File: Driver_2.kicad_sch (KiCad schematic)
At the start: 34 parts

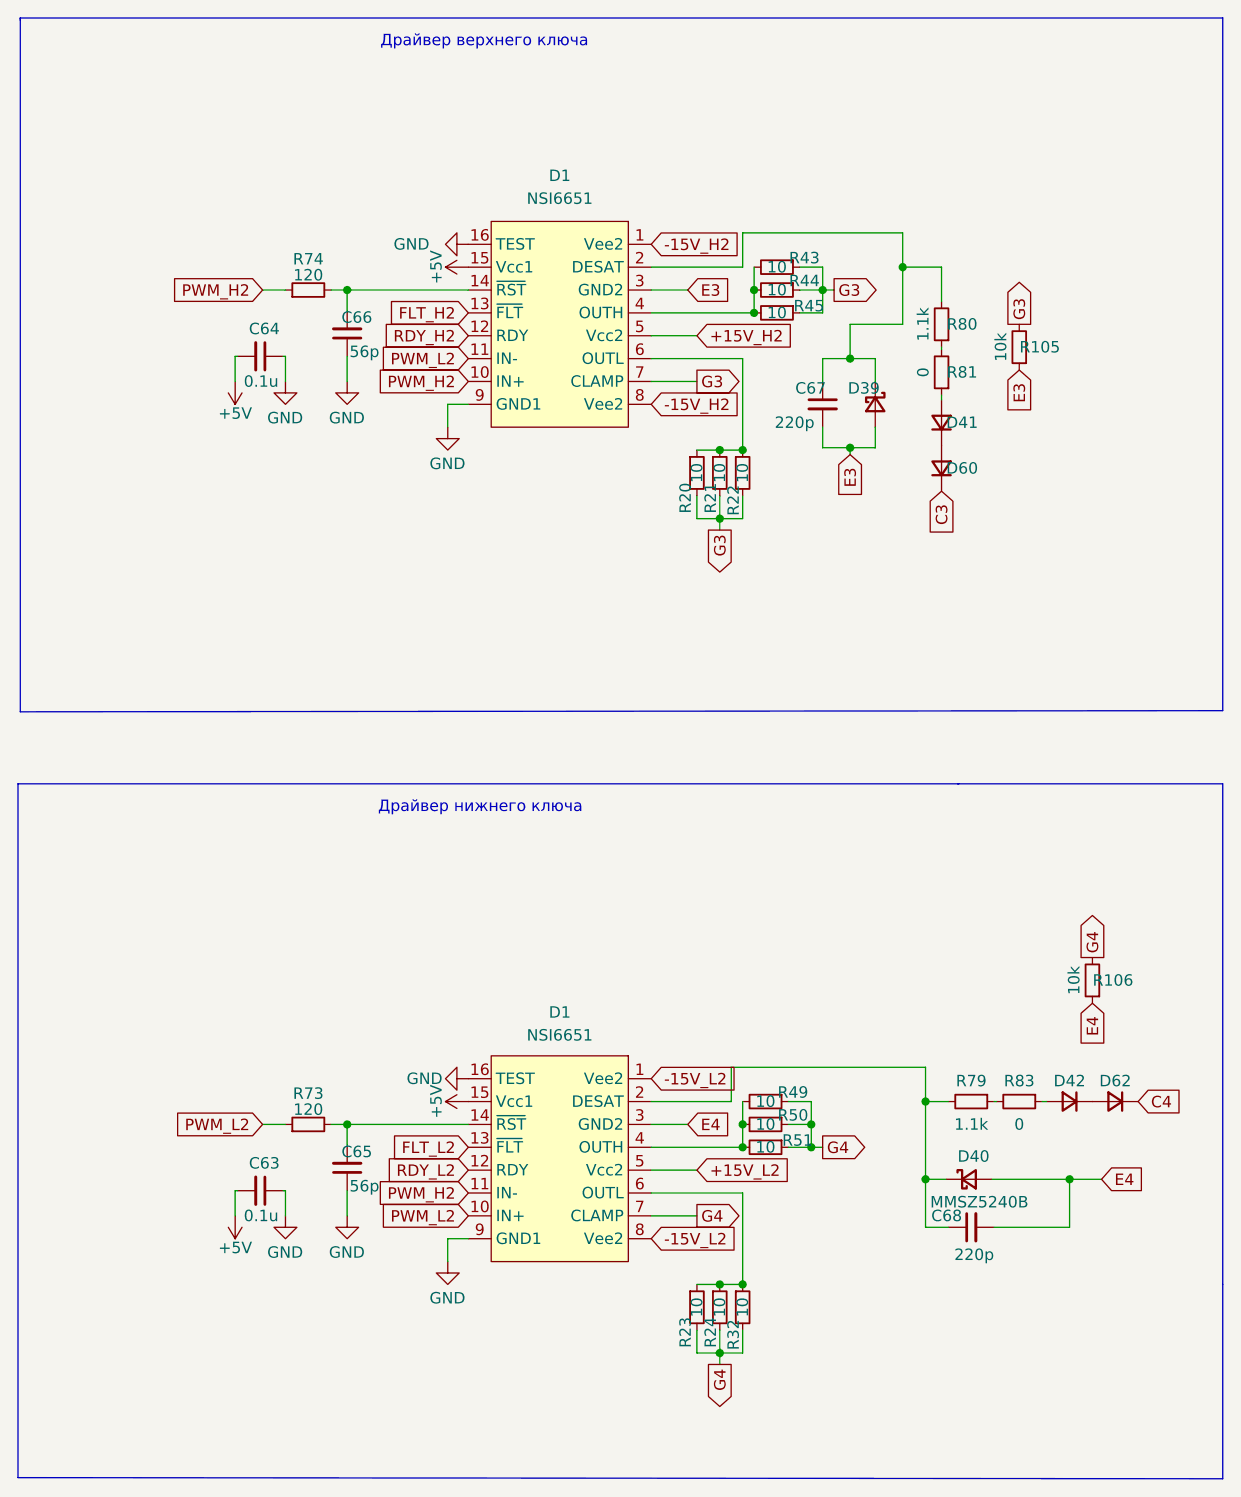
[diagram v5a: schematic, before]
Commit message: Развел стойку фазы А
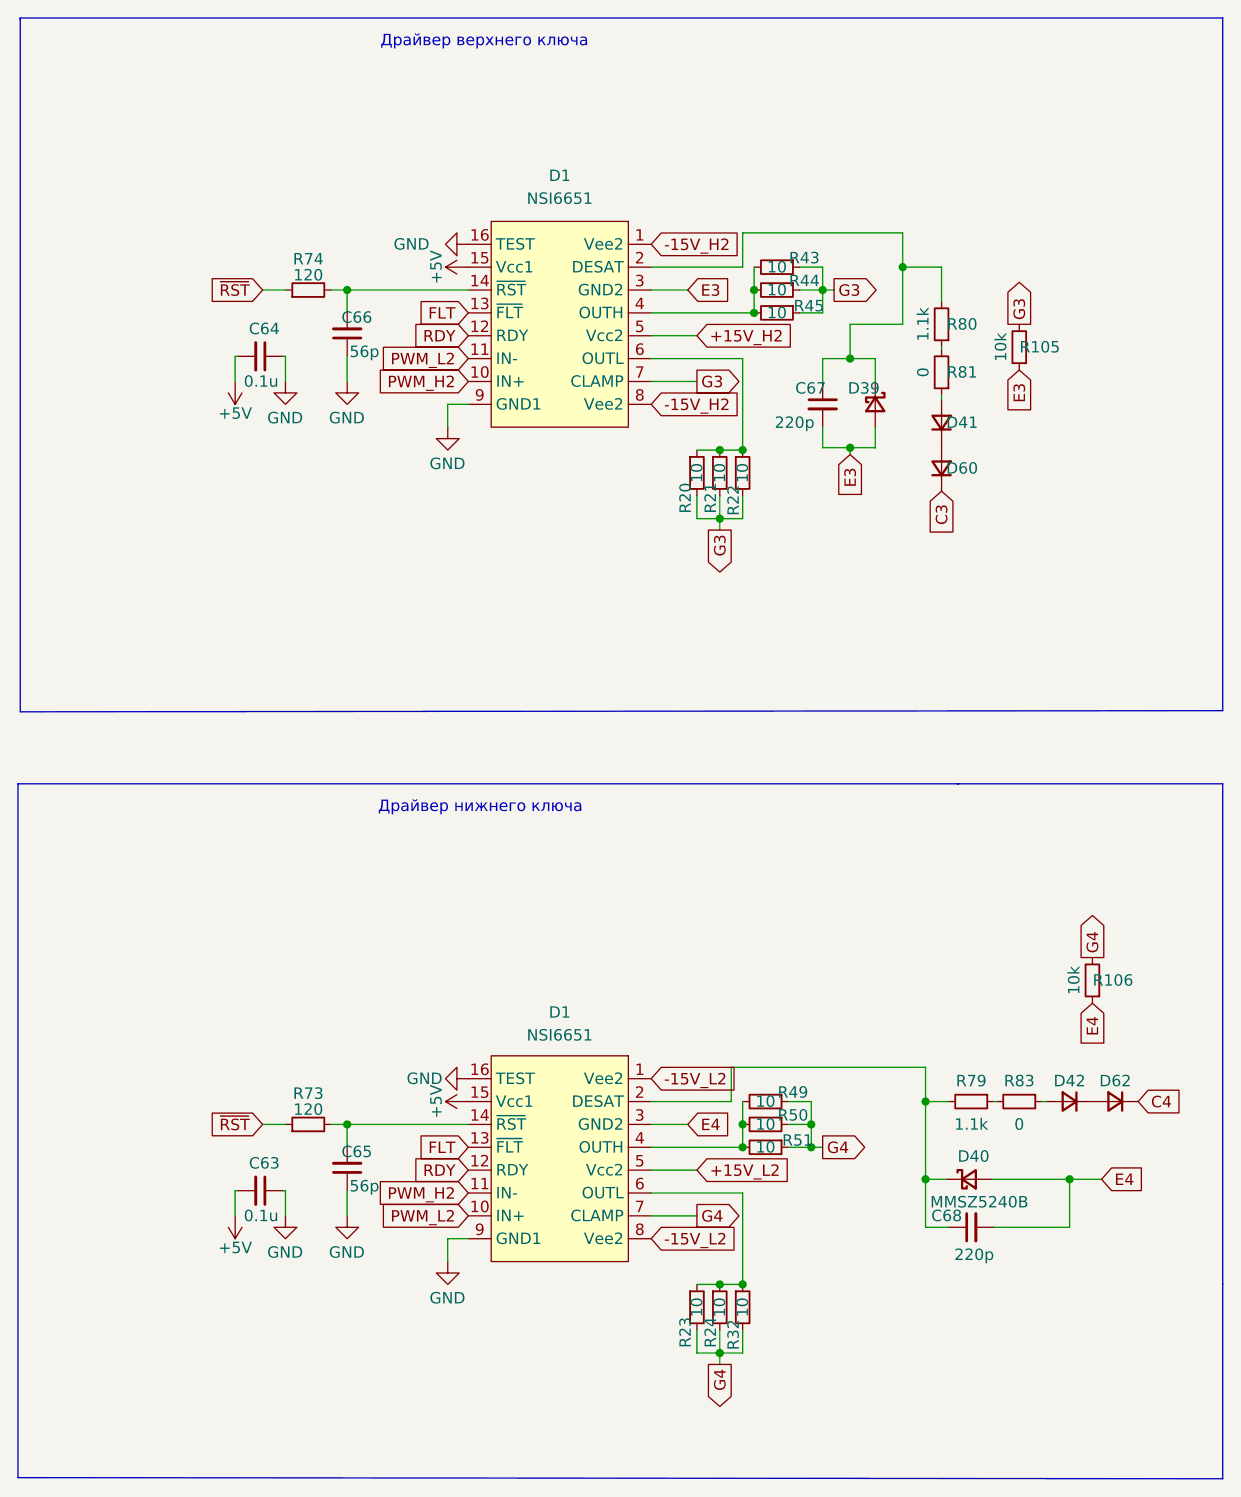
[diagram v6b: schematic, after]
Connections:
- net FLT_L2 is gone; now on net FLT: D1.13 (~{FLT})
- net RDY_L2 is gone; now on net RDY: D1.12 (RDY)
- net PWM_H2: no longer R74.1
- net PWM_L2: no longer R73.1
- net FLT_H2 renamed FLT
- net RDY_H2 renamed RDY
- new net ~{RST}: R73.1, R74.1
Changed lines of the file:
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@@
 		)
 	)
-	(global_label "FLT_H2"
+	(global_label "FLT"
 		(shape input)
 		(at 81.28 55.88 180)
@@
 		)
 		(property "Intersheetrefs" "${INTERSHEET_REFS}"
-			(at 72.275 55.8006 0)
+			(at 75.7206 55.88 0)
 			(effects
 				(font
@@
 		)
 	)
-	(global_label "FLT_L2"
+	(global_label "FLT"
 		(shape input)
 		(at 81.28 148.59 180)
@@
 		)
 		(property "Intersheetrefs" "${INTERSHEET_REFS}"
-			(at 72.5774 148.5106 0)
+			(at 75.7206 148.59 0)
 			(effects
 				(font
@@
 		)
 	)
-	(global_label "RDY_H2"
+	(global_label "RDY"
 		(shape input)
 		(at 81.28 58.42 180)
@@
 		)
 		(property "Intersheetrefs" "${INTERSHEET_REFS}"
-			(at 71.7307 58.3406 0)
+			(at 75.3384 58.42 0)
 			(effects
 				(font
@@
 		)
 	)
-	(global_label "RDY_L2"
+	(global_label "RDY"
 		(shape input)
 		(at 81.28 151.13 180)
@@
 		)
 		(property "Intersheetrefs" "${INTERSHEET_REFS}"
-			(at 72.0331 151.0506 0)
+			(at 75.3384 151.13 0)
 			(effects
 				(font
@@
 	(global_label "PWM_L2"
 		(shape input)
-		(at 58.42 146.05 180)
-		(fields_autoplaced yes)
-		(effects
-			(font
-				(size 1.27 1.27)
-			)
-			(justify right)
-		)
-		(property "Intersheetrefs" "${INTERSHEET_REFS}"
-			(at 48.6288 145.9706 0)
-			(effects
-				(font
-					(size 1.27 1.27)
-				)
-				(justify right)
-				(hide yes)
-			)
-		)
-	)
-	(global_label "PWM_L2"
-		(shape input)
 		(at 81.28 60.96 180)
 		(fields_autoplaced yes)
@@
 		)
 	)
-	(global_label "PWM_H2"
+	(global_label "~{RST}"
 		(shape input)
-		(at 58.42 53.34 180)
+		(at 58.42 146.05 180)
 		(fields_autoplaced yes)
 		(effects
@@
 		)
 		(property "Intersheetrefs" "${INTERSHEET_REFS}"
-			(at 48.3264 53.2606 0)
+			(at 52.605 146.05 0)
 			(effects
 				(font
@@
 		)
 	)
+	(global_label "~{RST}"
+		(shape input)
+		(at 58.42 53.34 180)
+		(fields_autoplaced yes)
+		(effects
+			(font
+				(size 1.27 1.27)
+			)
+			(justify right)
+		)
+		(property "Intersheetrefs" "${INTERSHEET_REFS}"
+			(at 52.605 53.34 0)
+			(effects
+				(font
+					(size 1.27 1.27)
+				)
+				(justify right)
+				(hide yes)
+			)
+		)
+	)
 	(global_label "-15V_H2"
 		(shape input)
@@
 		(on_board yes)
 		(dnp no)
-		(property "Reference" "#PWR181"
+		(property "Reference" "#PWR0181"
 			(at 55.372 152.4 0)
 			(effects
@@
 			(project "Adapter"
 				(path "/e63e39d7-6ac0-4ffd-8aa3-1841a4541b55/7be86f5d-dd1f-4f1b-8cd0-4746349973df"
-					(reference "#PWR181")
+					(reference "#PWR0181")
 					(unit 1)
 				)
@@
 		(on_board yes)
 		(dnp no)
-		(property "Reference" "#PWR176"
+		(property "Reference" "#PWR0176"
 			(at 85.09 50.8 0)
 			(effects
@@
 			(project "Adapter"
 				(path "/e63e39d7-6ac0-4ffd-8aa3-1841a4541b55/7be86f5d-dd1f-4f1b-8cd0-4746349973df"
-					(reference "#PWR176")
+					(reference "#PWR0176")
 					(unit 1)
 				)
@@
 		(on_board yes)
 		(dnp no)
-		(property "Reference" "#PWR175"
+		(property "Reference" "#PWR0175"
 			(at 55.372 59.69 0)
 			(effects
@@
 			(project "Adapter"
 				(path "/e63e39d7-6ac0-4ffd-8aa3-1841a4541b55/7be86f5d-dd1f-4f1b-8cd0-4746349973df"
-					(reference "#PWR175")
+					(reference "#PWR0175")
 					(unit 1)
 				)
@@
 		(on_board yes)
 		(dnp no)
-		(property "Reference" "#PWR182"
+		(property "Reference" "#PWR0182"
 			(at 85.09 143.51 0)
 			(effects
@@
 			(project "Adapter"
 				(path "/e63e39d7-6ac0-4ffd-8aa3-1841a4541b55/7be86f5d-dd1f-4f1b-8cd0-4746349973df"
-					(reference "#PWR182")
-					(unit 1)
-				)
+					(reference "#PWR0182")
+					(unit 1)
+				)

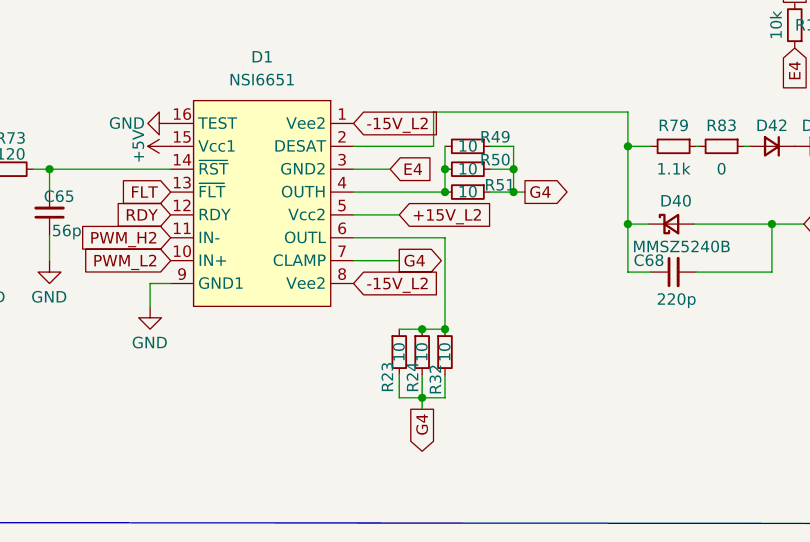
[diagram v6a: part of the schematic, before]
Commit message: Начал разводить вторую стойку
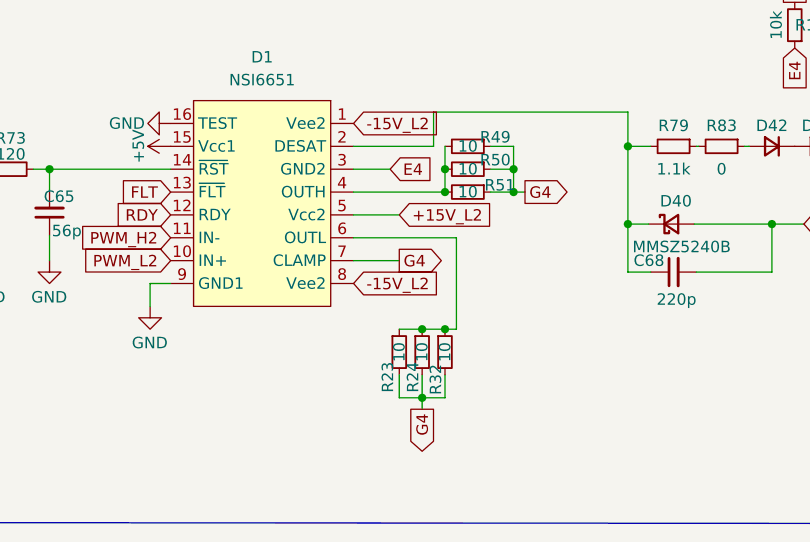
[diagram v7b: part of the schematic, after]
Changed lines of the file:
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@@
 	(wire
 		(pts
-			(xy 101.6 153.67) (xy 111.76 153.67)
+			(xy 101.6 153.67) (xy 113.03 153.67)
 		)
 		(stroke
@@
 	(wire
 		(pts
-			(xy 111.76 153.67) (xy 111.76 163.83)
+			(xy 113.03 153.67) (xy 113.03 163.83)
 		)
 		(stroke
@@
 		(pts
 			(xy 120.65 63.5) (xy 120.65 60.96)
+		)
+		(stroke
+			(width 0)
+			(type default)
+		)
+	)
+	(wire
+		(pts
+			(xy 113.03 163.83) (xy 111.76 163.83)
 		)
 		(stroke
@@
 		)
 		(property "Intersheetrefs" "${INTERSHEET_REFS}"
-			(at 112.2983 158.6706 0)
+			(at 112.8704 158.75 0)
 			(effects
 				(font

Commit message: Развел вторую стойку
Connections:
- net FLT renamed FLT_B
- net RDY renamed RDY_B
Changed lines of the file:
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@@
 		)
 	)
-	(global_label "FLT"
+	(global_label "FLT_B"
 		(shape input)
 		(at 81.28 55.88 180)
@@
 		)
 		(property "Intersheetrefs" "${INTERSHEET_REFS}"
-			(at 75.7206 55.88 0)
+			(at 72.9729 55.88 0)
 			(effects
 				(font
@@
 		)
 	)
-	(global_label "FLT"
+	(global_label "FLT_B"
 		(shape input)
 		(at 81.28 148.59 180)
@@
 		)
 		(property "Intersheetrefs" "${INTERSHEET_REFS}"
-			(at 75.7206 148.59 0)
+			(at 72.9729 148.59 0)
 			(effects
 				(font
@@
 		)
 	)
-	(global_label "RDY"
+	(global_label "RDY_B"
 		(shape input)
 		(at 81.28 58.42 180)
@@
 		)
 		(property "Intersheetrefs" "${INTERSHEET_REFS}"
-			(at 75.3384 58.42 0)
-			(effects
-				(font
-					(size 1.27 1.27)
-				)
-				(justify right)
-				(hide yes)
-			)
-		)
-	)
-	(global_label "RDY"
+			(at 72.4286 58.42 0)
+			(effects
+				(font
+					(size 1.27 1.27)
+				)
+				(justify right)
+				(hide yes)
+			)
+		)
+	)
+	(global_label "RDY_B"
 		(shape input)
 		(at 81.28 151.13 180)
@@
 		)
 		(property "Intersheetrefs" "${INTERSHEET_REFS}"
-			(at 75.3384 151.13 0)
-			(effects
-				(font
+			(at 72.4286 151.13 0)
+			(effects
+				(font
